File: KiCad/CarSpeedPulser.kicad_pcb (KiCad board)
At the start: 2 copper layers, 43.2 x 66 mm, 21 parts, among them P1 CONN_01X03, P2 CONN_01X05, Q1 2SK4017, SW1 RESET, SW2 UP, SW3 DOWN, U1 LPC810, U2 AQM0802A-RN-GBW, U3 XC6202P332TB

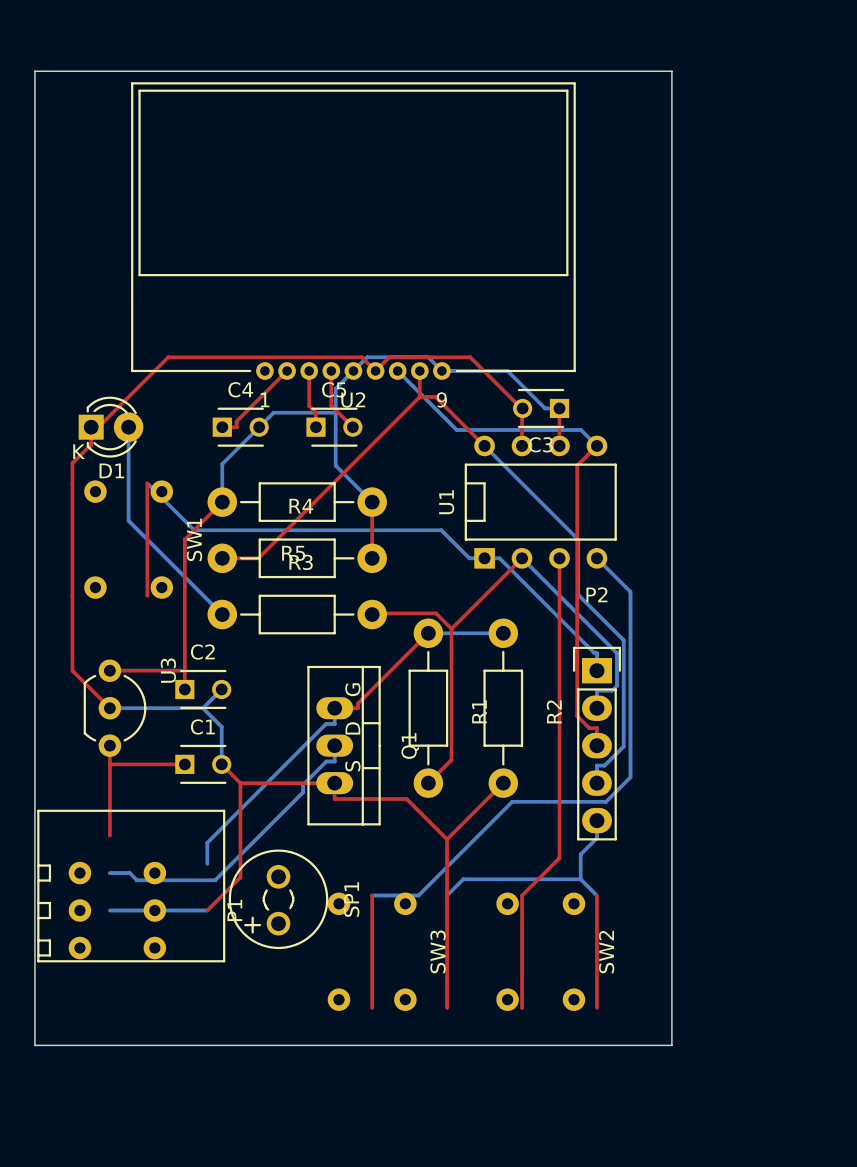
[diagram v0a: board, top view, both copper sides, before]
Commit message: Added footprint of piezo speaker.
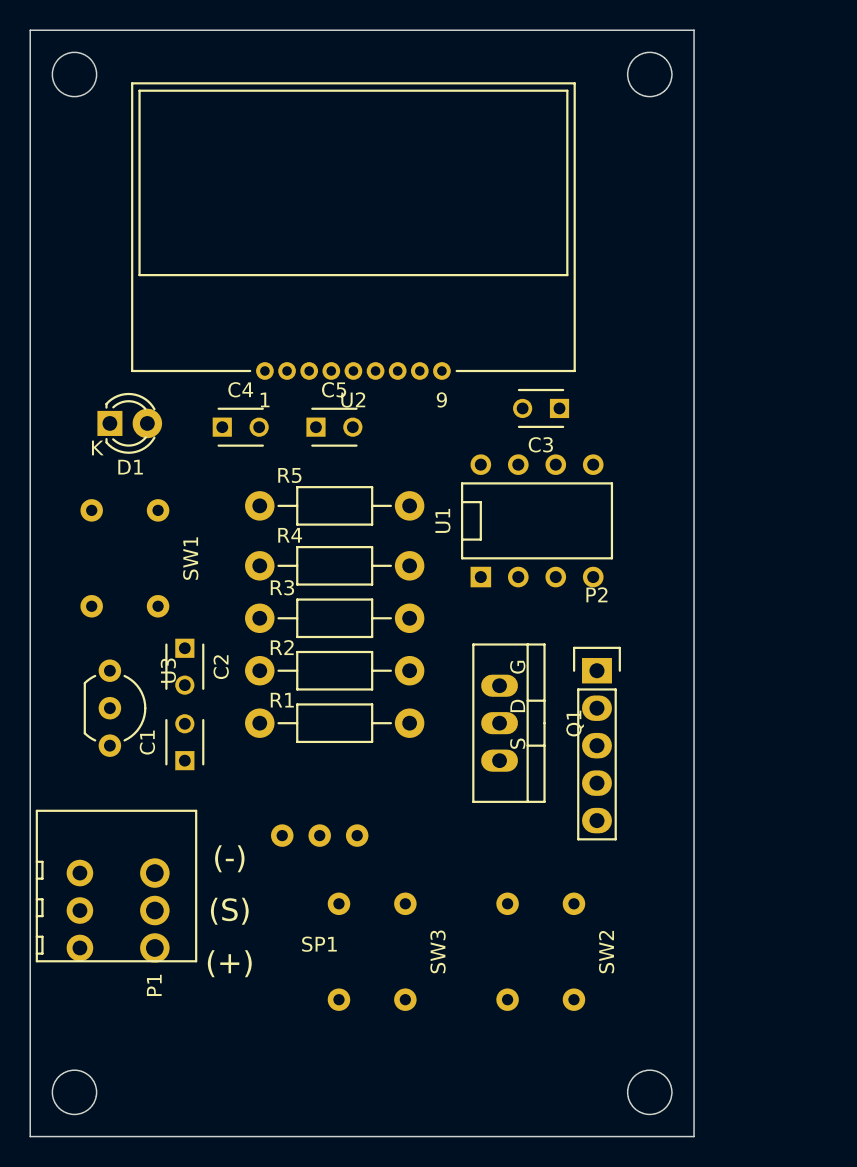
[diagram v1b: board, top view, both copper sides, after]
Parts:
- SP1: footprint Buzzers_Beepers:MagneticBuzzer_Kingstate_KCG0601 -> pulser:PKM13EPYH4000-A0
- moved R2 11.7 mm to (40.6, 58.4), turned to 0 degrees
- moved Q1 11.3 mm to (51.8, 62.0)
- moved R1 6.43 mm to (40.6, 62.0), turned to 0 degrees
- moved SP1 3.95 mm to (39.6, 69.6), turned to 0 degrees
- moved C2 2.79 mm to (30.5, 56.9), turned to 270 degrees
- moved R4 2.59 mm to (40.6, 51.3)
- moved R3 2.55 mm to (40.6, 54.9)
- moved R5 2.55 mm to (40.6, 47.2)
- moved D1 1.30 mm to (25.4, 41.7)
- moved SW1 1.30 mm to (26.4, 50.8)
- moved U1 1.30 mm to (54.4, 48.3)
- moved C1 0.25 mm to (30.5, 64.5), turned to 90 degrees
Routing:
- net GND: track 129.1 -> 0.00 mm
- net (no net): track 64.1 -> 0.00 mm
- net VDD: track 63.1 -> 0.00 mm
- net Net-(P2-Pad4): track 53.3 -> 0.00 mm
- net Net-(P2-Pad2): track 37.7 -> 0.00 mm
- net /SDA: track 37.4 -> 0.00 mm
- net Net-(SW3-Pad1): track 36.6 -> 0.00 mm
- net Net-(P2-Pad1): track 36.4 -> 0.00 mm
- net Net-(SW2-Pad1): track 31.5 -> 0.00 mm
- net Net-(D1-Pad2): track 15.3 -> 0.00 mm
- net Net-(Q1-Pad1): track 13.7 -> 0.00 mm
- net +12V: track 11.2 -> 0.00 mm
- net Net-(C4-Pad1): track 6.20 -> 0.00 mm
- net Net-(C5-Pad2): track 4.41 -> 0.00 mm
- net Net-(C5-Pad1): track 4.00 -> 0.00 mm
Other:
- board size 43.2 x 66 mm -> 45 x 75 mm
- board text added: "(+)"
- board text added: "(-)"
- board text added: "(S)"

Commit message: Replaced voltage regulator to SMD type.
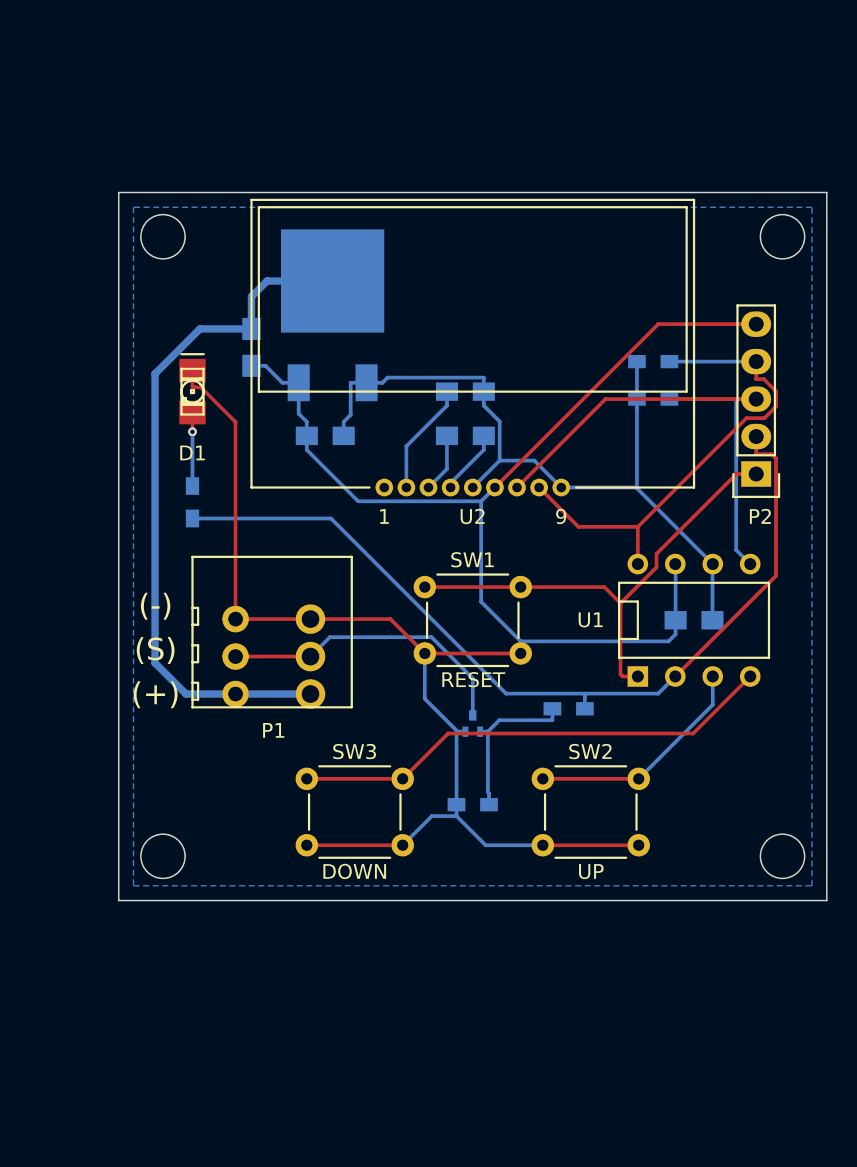
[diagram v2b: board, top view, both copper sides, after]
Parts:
- removed SP1: PiezoSpk, pulser:PKM13EPYH4000-A0
- C1, C2, C4, C5: footprint Capacitors_ThroughHole:C_Disc_D3_P2.5 -> Capacitors_SMD:C_0805_HandSoldering; moved to B.Cu
- C3: value 0.1u -> 1u; footprint Capacitors_ThroughHole:C_Disc_D3_P2.5 -> Capacitors_SMD:C_0805_HandSoldering; moved to B.Cu
- D1: footprint LEDs:LED-3MM -> favorites:LED-1206
- Q1: value 2SK4017 -> RUE002N02; footprint Transistors_TO-220:TO-220_FET-GDS_Vertical -> favorites:EMT3; moved to B.Cu
- R1, R4, R5: footprint Resistors_ThroughHole:Resistor_Horizontal_RM10mm -> Resistors_SMD:R_0603_HandSoldering; moved to B.Cu
- R2: value 100k -> 1M; footprint Resistors_ThroughHole:Resistor_Horizontal_RM10mm -> Resistors_SMD:R_0603_HandSoldering; moved to B.Cu
- R3: value 100 -> 680; footprint Resistors_ThroughHole:Resistor_Horizontal_RM10mm -> Resistors_SMD:R_0603_HandSoldering; moved to B.Cu
- U3: value XC6202P332TB -> NJU7223DL1-33; footprint Housings_TO-92:TO-92_Inline_Wide -> favorites:TO-252; moved to B.Cu
- moved C2 34.6 mm to (65.0, 55.0), turned to 180 degrees
- moved U3 30.4 mm to (40.5, 32.0), turned to 180 degrees
- moved C1 28.4 mm to (35.0, 36.5), turned to 270 degrees
- moved R4 25.6 mm to (62.2, 37.5), turned to 180 degrees
- moved SW1 24.0 mm to (50.0, 55.0), turned to 0 degrees
- moved R5 22.8 mm to (62.2, 40.0)
- moved P1 20.2 mm to (39.0, 60.0)
- moved P2 17.2 mm to (69.2, 45.1), turned to 180 degrees
- moved C4 16.7 mm to (49.5, 39.5)
- moved C3 16.0 mm to (40.0, 42.5)
- moved R1 15.9 mm to (56.5, 61.0)
- moved R2 13.0 mm to (50.0, 67.5), turned to 180 degrees
- moved U1 12.6 mm to (65.0, 55.0)
- moved R3 12.4 mm to (31.0, 47.0), turned to 270 degrees
- moved U2 11.3 mm to (50.0, 46.0)
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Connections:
- net Net-(C4-Pad1) renamed /VOUT
- net Net-(C5-Pad1) renamed /CAP1N
- net Net-(C5-Pad2) renamed /CAP1P
- net Net-(P2-Pad1) renamed /#RST
- net Net-(P2-Pad2) renamed /PIO0_4
- net Net-(P2-Pad4) renamed /SCL
- net Net-(SW2-Pad1) renamed /PIO0_3
- net Net-(SW3-Pad1) renamed /PIO0_2
- R1 pad 1: Net-(Q1-Pad1) -> /GATE
- R2 pad 1: Net-(Q1-Pad1) -> /GATE
- R5 pad 1: VDD -> /SDA
- U3 pad 2: GND -> +12V
- U3 pad 3: +12V -> GND
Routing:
- net GND: track 0.00 -> 147.5 mm
- net /PIO0_4: track 0.00 -> 59.4 mm
- net VDD: track 0.00 -> 51.4 mm
- net +12V: track 0.00 -> 46.9 mm
- net /SDA: track 0.00 -> 36.2 mm
- net /#RST: track 0.00 -> 33.1 mm
- net /PIO0_2: track 0.00 -> 32.9 mm
- net /SCL: track 0.00 -> 32.9 mm
- net /PULSE: track 0.00 -> 20.3 mm
- net /PIO0_3: track 0.00 -> 15.5 mm
- net /GATE: track 0.00 -> 11.0 mm
- net /VOUT: track 0.00 -> 7.64 mm
- net Net-(D1-Pad2): track 0.00 -> 4.98 mm, vias 0 -> 1
- net /CAP1P: track 0.00 -> 4.43 mm
- net /CAP1N: track 0.00 -> 4.02 mm
- added copper zone on B.Cu, net GND
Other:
- board size 45 x 75 mm -> 48 x 48 mm
- net class Power added: clearance 0.2, trace_width 0.5, via_dia 0.6, via_drill 0.4
- board text added: "JIS D 5601 Pulse Generator Rev.2"

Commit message: Added diodes, registers and a voltage detector.
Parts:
- added D2: 1N4148W, Diodes_SMD:SOD-123, B.Cu at (37.7, 47.0)
- added D3: 1N4148W, Diodes_SMD:SOD-123, B.Cu at (37.7, 50.9)
- added R6: 1M, Resistors_SMD:R_0603_HandSoldering, B.Cu at (56.8, 49.6)
- added U4: BD45231G, favorites:SSOP5_Handsoldering, B.Cu at (61.9, 45.5)
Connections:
- net /PULSE renamed /D
- C1 pad 1: +12V -> /Vin
- C1 pad 2: GND -> /VSS
- C2 pad 2: GND -> /VSS
- C3 pad 2: GND -> /VSS
- D1 pad 1: GND -> /VSS
- P1 pad 3: GND -> Net-(D3-Pad1)
- P2 pad 5: GND -> /VSS
- Q1 pad 1: GND -> /VSS
- R2 pad 2: GND -> /VSS
- SW1 pad 2: GND -> /VSS
- SW2 pad 2: GND -> /VSS
- SW3 pad 2: GND -> /VSS
- U1 pad 7: GND -> /VSS
- U2 pad 6: GND -> /VSS
- U3 pad 2: +12V -> /Vin
- U3 pad 3: GND -> /VSS
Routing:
- net /VSS: track 0.00 -> 160.0 mm
- net GND: track 147.5 -> 0.00 mm
- net +12V: track 46.9 -> 19.7 mm
- net /Vin: track 0.00 -> 22.6 mm
- net /#RST: track 33.1 -> 47.3 mm
- net /PIO0_4: track 59.4 -> 71.0 mm
- net Net-(D3-Pad1): track 0.00 -> 9.85 mm
- net VDD: track 51.4 -> 60.6 mm
- net /SCL: track 32.9 -> 35.6 mm
- net /D: track 20.3 -> 17.8 mm, vias 0 -> 1
- removed copper zone on B.Cu, net GND
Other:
- net class Default: trace_width 0.25 -> 0.5
- board text added: "JIS D 5601 Pulse Generator Rev.3"
- board text removed: "JIS D 5601 Pulse Generator Rev.2"
